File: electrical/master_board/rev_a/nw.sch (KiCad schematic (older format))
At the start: 22 parts

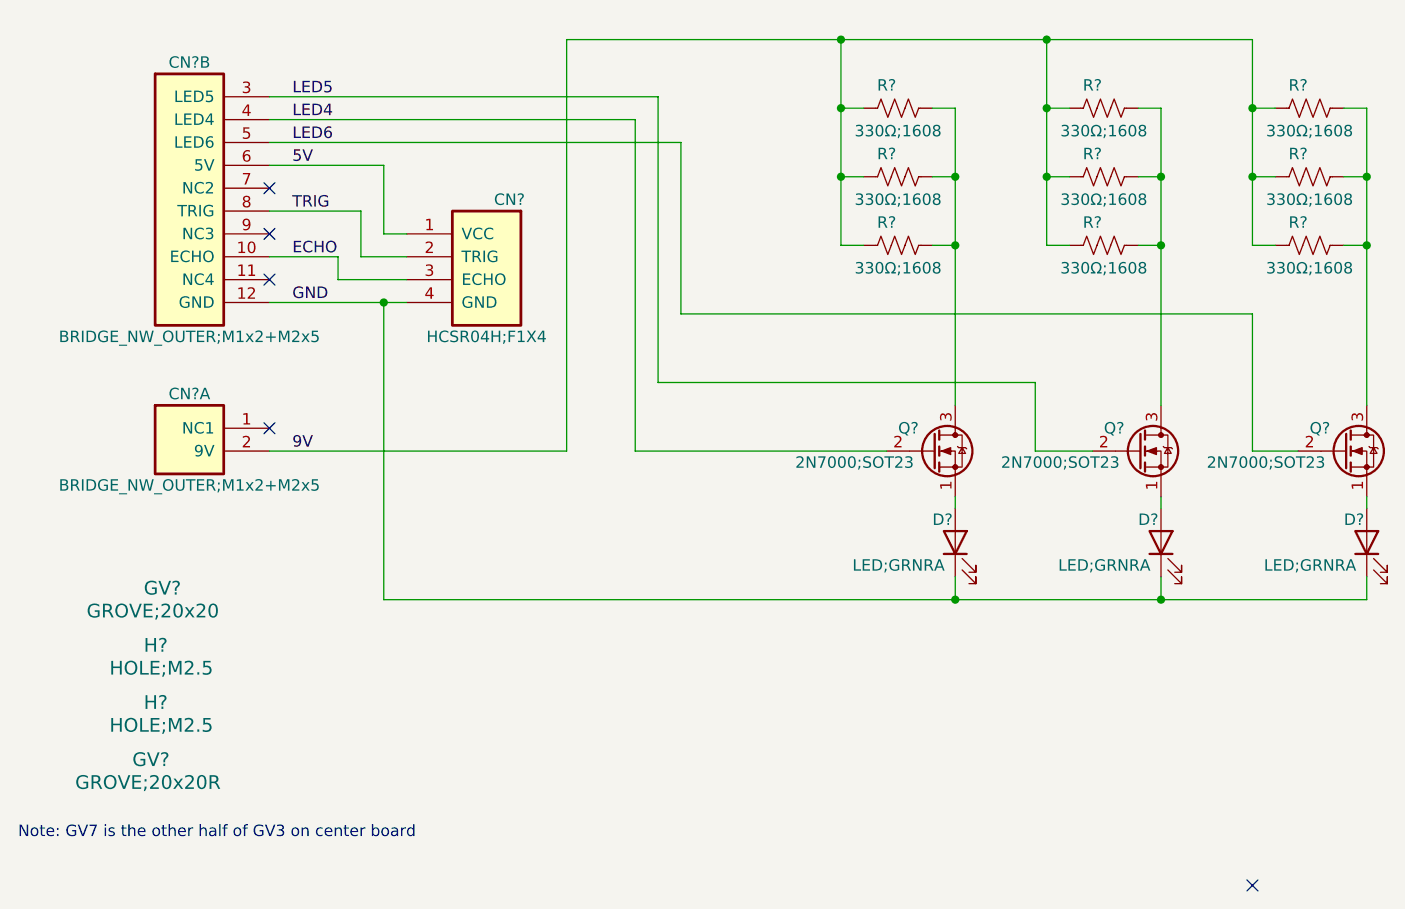
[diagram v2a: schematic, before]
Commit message: Reworked Sonars, Servers, and LED's schematics.
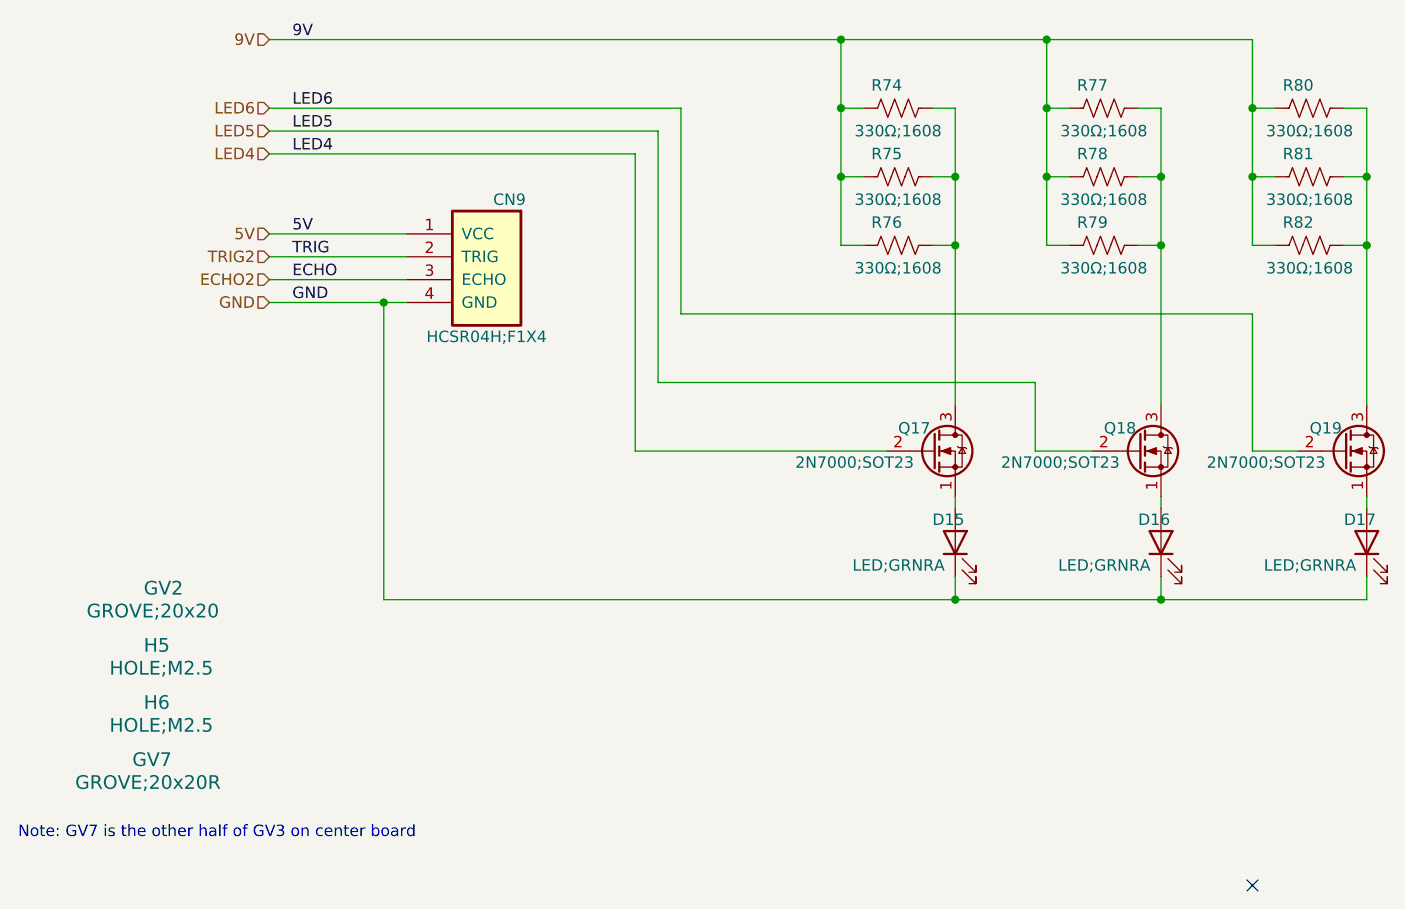
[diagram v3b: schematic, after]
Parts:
- removed CN? (x2): BRIDGE_NW_OUTER;M1x2+M2x5, HR2:BRIDGE_NW_OUTER_M1x2+M2x5, symbol HR2:BRIDGE_NW_OUTER;M1x2+M2x5
- gave numbers to parts that had none: 20
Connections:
- net ECHO renamed ECHO2
- net TRIG renamed TRIG2
- no-connect marks 5 -> 1
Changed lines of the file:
@@
 $Descr A 11000 8500
 encoding utf-8
-Sheet 12 12
-Title "HR2 NE PCB"
-Date "2020-06-13"
+Sheet 11 11
+Title "HR2 Master Board"
+Date "2020-10-03"
 Rev "A"
-Comp "Homebrew Robotics Club"
-Comment1 ""
-Comment2 ""
+Comp "HomeBrew Robotics Club"
+Comment1 "Copyright © 2020 by HomeBrew Robotics Club "
+Comment2 "MIT License"
 Comment3 ""
 Comment4 ""
 $EndDescr
 $Comp
-L HR2:HOLE;M2.5 H?
+L HR2:HOLE;M2.5 H6
 U 1 1 5F2F7B9C
 P 1500 5550
-F 0 "H?" H 1450 5600 60  0000 L CNN
+F 0 "H6" H 1450 5600 60  0000 L CNN
 F 1 "HOLE;M2.5" H 1300 5500 60  0000 L CNN
 F 2 "MountingHole:MountingHole_2.7mm_M2.5" H 1700 5600 60  0001 L CNN
@@
 $EndComp
 $Comp
-L HR2:HOLE;M2.5 H?
+L HR2:HOLE;M2.5 H5
 U 1 1 5F2F8125
 P 1500 5300
-F 0 "H?" H 1450 5350 60  0000 L CNN
+F 0 "H5" H 1450 5350 60  0000 L CNN
 F 1 "HOLE;M2.5" H 1300 5250 60  0000 L CNN
 F 2 "MountingHole:MountingHole_2.7mm_M2.5" H 1700 5350 60  0001 L CNN
@@
 $EndComp
 $Comp
-L HR2:GROVE;20x20 GV?
+L HR2:GROVE;20x20 GV2
 U 1 1 5F2F999C
 P 1500 5050
-F 0 "GV?" H 1450 5100 60  0000 L CNN
+F 0 "GV2" H 1450 5100 60  0000 L CNN
 F 1 "GROVE;20x20" H 1200 5000 60  0000 L CNN
 F 2 "HR2:GROVE20x20" H 1700 5100 60  0001 L CNN
@@
 $EndComp
 $Comp
-L HR2:GROVE;20x20R GV?
+L HR2:GROVE;20x20R GV7
 U 1 1 5F303BB1
 P 1500 5800
-F 0 "GV?" H 1400 5850 60  0000 L CNN
+F 0 "GV7" H 1400 5850 60  0000 L CNN
 F 1 "GROVE;20x20R" H 1150 5750 60  0000 L CNN
 F 2 "HR2:GROVE20x20R" H 1700 5850 60  0001 L CNN
@@
 Note: GV7 is the other half of GV3 on center board
 $Comp
-L Device:LED D?
+L Device:LED D15
 U 1 1 5F30BC5B
 P 5000 4800
-F 0 "D?" V 5100 4900 50  0000 R CNN
+F 0 "D15" V 5100 4900 50  0000 R CNN
 F 1 "LED;GRNRA" V 4900 5250 50  0000 R CNN
 F 2 "HR2:LED_GRNRA" H 5000 4800 50  0001 C CNN
@@
 $EndComp
 $Comp
-L Device:LED D?
+L Device:LED D16
 U 1 1 5F30DD43
 P 5900 4800
-F 0 "D?" V 6000 4900 50  0000 R CNN
+F 0 "D16" V 6000 4900 50  0000 R CNN
 F 1 "LED;GRNRA" V 5800 5250 50  0000 R CNN
 F 2 "HR2:LED_GRNRA" H 5900 4800 50  0001 C CNN
@@
 $EndComp
 $Comp
-L Device:LED D?
+L Device:LED D17
 U 1 1 5F30E439
 P 6800 4800
-F 0 "D?" V 6900 4900 50  0000 R CNN
+F 0 "D17" V 6900 4900 50  0000 R CNN
 F 1 "LED;GRNRA" V 6700 5250 50  0000 R CNN
 F 2 "HR2:LED_GRNRA" H 6800 4800 50  0001 C CNN
@@
 	0    -1   -1   0
 $EndComp
-$Comp
-L HR2:BRIDGE_NW_OUTER;M1x2+M2x5 CN?
-U 1 1 5F3877C6
-P 1300 4300
-F 0 "CN?" H 1650 4450 50  0000 C CNN
-F 1 "BRIDGE_NW_OUTER;M1x2+M2x5" H 1650 4050 50  0000 C CNN
-F 2 "HR2:BRIDGE_NW_OUTER_M1x2+M2x5" H 1500 4350 60  0001 L CNN
-F 3 "" H 1500 4150 60  0001 L CNN
-F 4 "NW Outer Bridge Connectors" H 1500 4050 60  0001 L CNN "Field5"
-	1    1300 4300
-	1    0    0    -1
-$EndComp
-$Comp
-L HR2:BRIDGE_NW_OUTER;M1x2+M2x5 CN?
-U 2 1 5F389BE1
-P 1300 2850
-F 0 "CN?" H 1650 3000 50  0000 C CNN
-F 1 "BRIDGE_NW_OUTER;M1x2+M2x5" H 1650 1800 50  0000 C CNN
-F 2 "HR2:BRIDGE_NW_OUTER_M1x2+M2x5" H 1500 2900 60  0001 L CNN
-F 3 "" H 1500 2700 60  0001 L CNN
-F 4 "NW Outer Bridge Connectors" H 1500 2600 60  0001 L CNN "Field5"
-	2    1300 2850
-	1    0    0    -1
-$EndComp
 Text Label 2100 3750 0    50   ~ 0
 GND
 $Comp
-L Transistor_FET:2N7000 Q?
+L Transistor_FET:2N7000 Q17
 U 1 1 5F433B12
 P 4900 4400
-F 0 "Q?" H 4750 4500 50  0000 L CNN
+F 0 "Q17" H 4750 4500 50  0000 L CNN
 F 1 "2N7000;SOT23" H 4300 4350 50  0000 L CNN
 F 2 "Package_TO_SOT_SMD:SOT-23" H 5100 4325 50  0001 L CIN
@@
 $EndComp
 $Comp
-L Device:R_US R?
+L Device:R_US R76
 U 1 1 5F434F01
 P 4750 3500
-F 0 "R?" V 4650 3450 50  0000 C CNN
+F 0 "R76" V 4650 3450 50  0000 C CNN
 F 1 "330Ω;1608" V 4850 3500 50  0000 C CNN
 F 2 "Resistor_SMD:R_0603_1608Metric" V 4790 3490 50  0001 C CNN
@@
 $EndComp
 $Comp
-L Device:R_US R?
+L Device:R_US R75
 U 1 1 5F437EB2
 P 4750 3200
-F 0 "R?" V 4650 3150 50  0000 C CNN
+F 0 "R75" V 4650 3150 50  0000 C CNN
 F 1 "330Ω;1608" V 4850 3200 50  0000 C CNN
 F 2 "Resistor_SMD:R_0603_1608Metric" V 4790 3190 50  0001 C CNN
@@
 $EndComp
 $Comp
-L Device:R_US R?
+L Device:R_US R74
 U 1 1 5F43808D
 P 4750 2900
-F 0 "R?" V 4650 2850 50  0000 C CNN
+F 0 "R74" V 4650 2850 50  0000 C CNN
 F 1 "330Ω;1608" V 4850 2900 50  0000 C CNN
 F 2 "Resistor_SMD:R_0603_1608Metric" V 4790 2890 50  0001 C CNN
@@
 Connection ~ 4500 2900
 $Comp
-L Transistor_FET:2N7000 Q?
+L Transistor_FET:2N7000 Q18
 U 1 1 5F43B291
 P 5800 4400
-F 0 "Q?" H 5650 4500 50  0000 L CNN
+F 0 "Q18" H 5650 4500 50  0000 L CNN
 F 1 "2N7000;SOT23" H 5200 4350 50  0000 L CNN
 F 2 "Package_TO_SOT_SMD:SOT-23" H 6000 4325 50  0001 L CIN
@@
 $EndComp
 $Comp
-L Device:R_US R?
+L Device:R_US R79
 U 1 1 5F43B29B
 P 5650 3500
-F 0 "R?" V 5550 3450 50  0000 C CNN
+F 0 "R79" V 5550 3450 50  0000 C CNN
 F 1 "330Ω;1608" V 5750 3500 50  0000 C CNN
 F 2 "Resistor_SMD:R_0603_1608Metric" V 5690 3490 50  0001 C CNN
@@
 $EndComp
 $Comp
-L Device:R_US R?
+L Device:R_US R78
 U 1 1 5F43B2A5
 P 5650 3200
-F 0 "R?" V 5550 3150 50  0000 C CNN
+F 0 "R78" V 5550 3150 50  0000 C CNN
 F 1 "330Ω;1608" V 5750 3200 50  0000 C CNN
 F 2 "Resistor_SMD:R_0603_1608Metric" V 5690 3190 50  0001 C CNN
@@
 $EndComp
 $Comp
-L Device:R_US R?
+L Device:R_US R77
 U 1 1 5F43B2AF
 P 5650 2900
-F 0 "R?" V 5550 2850 50  0000 C CNN
+F 0 "R77" V 5550 2850 50  0000 C CNN
 F 1 "330Ω;1608" V 5750 2900 50  0000 C CNN
 F 2 "Resistor_SMD:R_0603_1608Metric" V 5690 2890 50  0001 C CNN
@@
 Connection ~ 5400 2900
 $Comp
-L Transistor_FET:2N7000 Q?
+L Transistor_FET:2N7000 Q19
 U 1 1 5F4407CF
 P 6700 4400
-F 0 "Q?" H 6550 4500 50  0000 L CNN
+F 0 "Q19" H 6550 4500 50  0000 L CNN
 F 1 "2N7000;SOT23" H 6100 4350 50  0000 L CNN
 F 2 "Package_TO_SOT_SMD:SOT-23" H 6900 4325 50  0001 L CIN
@@
 $EndComp
 $Comp
-L Device:R_US R?
+L Device:R_US R82
 U 1 1 5F4407D9
 P 6550 3500
-F 0 "R?" V 6450 3450 50  0000 C CNN
+F 0 "R82" V 6450 3450 50  0000 C CNN
 F 1 "330Ω;1608" V 6650 3500 50  0000 C CNN
 F 2 "Resistor_SMD:R_0603_1608Metric" V 6590 3490 50  0001 C CNN
@@
 $EndComp
 $Comp
-L Device:R_US R?
+L Device:R_US R81
 U 1 1 5F4407E3
 P 6550 3200
-F 0 "R?" V 6450 3150 50  0000 C CNN
+F 0 "R81" V 6450 3150 50  0000 C CNN
 F 1 "330Ω;1608" V 6650 3200 50  0000 C CNN
 F 2 "Resistor_SMD:R_0603_1608Metric" V 6590 3190 50  0001 C CNN
@@
 $EndComp
 $Comp
-L Device:R_US R?
+L Device:R_US R80
 U 1 1 5F4407ED
 P 6550 2900
-F 0 "R?" V 6450 2850 50  0000 C CNN
+F 0 "R80" V 6450 2850 50  0000 C CNN
 F 1 "330Ω;1608" V 6650 2900 50  0000 C CNN
 F 2 "Resistor_SMD:R_0603_1608Metric" V 6590 2890 50  0001 C CNN
@@
 	2500 5050 5000 5050
 Connection ~ 5000 5050
-Text Label 2100 2850 0    50   ~ 0
+Text Label 2100 3000 0    50   ~ 0
 LED5
 Wire Wire Line
 	5350 4100 5350 4400
-Text Label 2100 2950 0    50   ~ 0
+Text Label 2100 3100 0    50   ~ 0
 LED4
-Text Label 2100 3050 0    50   ~ 0
+Text Label 2100 2900 0    50   ~ 0
 LED6
-Text Label 2100 3350 0    50   ~ 0
+Text Label 2100 3550 0    50   ~ 0
 TRIG
-Text Label 2100 3150 0    50   ~ 0
+Text Label 2100 3450 0    50   ~ 0
 5V
-Text Label 2100 3550 0    50   ~ 0
+Text Label 2100 3650 0    50   ~ 0
 ECHO
 NoConn ~ 6300 6300
@@
 	2500 3750 2500 5050
 $Comp
-L HR2:HCSR04H;F1X4 CN?
+L HR2:HCSR04H;F1X4 CN9
 U 1 1 5F0B8A7B
 P 3300 3450
-F 0 "CN?" H 3550 3600 50  0000 C CNN
+F 0 "CN9" H 3550 3600 50  0000 C CNN
 F 1 "HCSR04H;F1X4" H 3650 3000 50  0000 C CNN
 F 2 "HR2:HCSR04_F1x4H" H 3500 3500 60  0001 L CNN
@@
 	2600 3750 2500 3750
 Connection ~ 4500 2600
-Text Label 2100 4400 0    50   ~ 0
+Text Label 2100 2600 0    50   ~ 0
 9V
-Wire Wire Line
-	2000 4400 3300 4400
-Wire Wire Line
-	3300 4400 3300 2600
-Wire Wire Line
-	3300 2600 4500 2600
 Wire Wire Line
 	2000 3750 2500 3750
 Connection ~ 2500 3750
 Wire Wire Line
-	2000 3550 2300 3550
-Wire Wire Line
-	2300 3550 2300 3650
-Wire Wire Line
-	2300 3650 2600 3650
-Wire Wire Line
-	2000 3350 2400 3350
-Wire Wire Line
-	2400 3350 2400 3550
-Wire Wire Line
-	2400 3550 2600 3550
-Wire Wire Line
-	2600 3450 2500 3450
-Wire Wire Line
-	2500 3450 2500 3150
-Wire Wire Line
-	2500 3150 2000 3150
-Wire Wire Line
-	2000 2950 3600 2950
-Wire Wire Line
-	3600 2950 3600 4400
+	2000 3100 3600 3100
+Wire Wire Line
+	3600 3100 3600 4400
 Wire Wire Line
 	3600 4400 4700 4400
 Wire Wire Line
-	2000 2850 3700 2850
-Wire Wire Line
-	3700 2850 3700 4100
+	2000 3000 3700 3000
+Wire Wire Line
+	3700 3000 3700 4100
 Wire Wire Line
 	3700 4100 5350 4100
 Wire Wire Line
-	2000 3050 3800 3050
-Wire Wire Line
-	3800 3050 3800 3800
+	2000 2900 3800 2900
+Wire Wire Line
+	3800 2900 3800 3800
 Wire Wire Line
 	3800 3800 6300 3800
-NoConn ~ 2000 3250
-NoConn ~ 2000 3450
-NoConn ~ 2000 3650
-NoConn ~ 2000 4300
+Text HLabel 2000 3000 0    50   Input ~ 0
+LED5
+Text HLabel 2000 3100 0    50   Input ~ 0
+LED4
+Text HLabel 2000 2900 0    50   Input ~ 0
+LED6
+Text HLabel 2000 3450 0    50   Input ~ 0
+5V
+Text HLabel 2000 3550 0    50   Input ~ 0
+TRIG2
+Text HLabel 2000 3650 0    50   Input ~ 0
+ECHO2
+Text HLabel 2000 3750 0    50   Input ~ 0
+GND
+Wire Wire Line
+	2000 3650 2600 3650
+Wire Wire Line
+	2000 3550 2600 3550
+Wire Wire Line
+	2000 3450 2600 3450
+Wire Wire Line
+	2000 2600 4500 2600
+Text HLabel 2000 2600 0    50   Input ~ 0
+9V
 $EndSCHEMATC
